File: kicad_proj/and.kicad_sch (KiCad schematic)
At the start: 2 parts, among them U7 SN74AHC1G08DBVR

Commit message: checked root, dc dc and rpi sheets
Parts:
- renumbered C16 to C17, U7 to U8
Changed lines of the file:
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@@
 		(dnp no)
 		(fields_autoplaced yes)
-		(property "Reference" "#PWR37"
+		(property "Reference" "#PWR38"
 			(at 139.7 92.71 0)
 			(effects
@@
 			(project "rpi_power_warden_hat"
 				(path "/8692c5de-a943-41e8-8e29-f6c5e99cda34/67c50b5c-a842-43c6-be7c-97015e7e2432"
-					(reference "#PWR39")
+					(reference "#PWR38")
 					(unit 1)
 				)
 				(path "/8692c5de-a943-41e8-8e29-f6c5e99cda34/fdee896d-a6fa-4854-a7d2-28092c85ff44"
-					(reference "#PWR37")
+					(reference "#PWR36")
 					(unit 1)
 				)
@@
 		(dnp no)
 		(fields_autoplaced yes)
-		(property "Reference" "#PWR38"
+		(property "Reference" "#PWR39"
 			(at 148.59 115.57 0)
 			(effects
@@
 			(project "rpi_power_warden_hat"
 				(path "/8692c5de-a943-41e8-8e29-f6c5e99cda34/67c50b5c-a842-43c6-be7c-97015e7e2432"
-					(reference "#PWR40")
+					(reference "#PWR39")
 					(unit 1)
 				)
 				(path "/8692c5de-a943-41e8-8e29-f6c5e99cda34/fdee896d-a6fa-4854-a7d2-28092c85ff44"
-					(reference "#PWR38")
+					(reference "#PWR37")
 					(unit 1)
 				)
@@
 		(on_board yes)
 		(dnp no)
-		(property "Reference" "C16"
+		(property "Reference" "C17"
 			(at 135.382 82.55 90)
 			(effects
@@
 		(dnp no)
 		(fields_autoplaced yes)
-		(property "Reference" "U7"
+		(property "Reference" "U8"
 			(at 166.37 93.0908 0)
 			(effects

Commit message: re-annotate schematic
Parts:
- renumbered U8 to U10
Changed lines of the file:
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@@
 		(dnp no)
 		(fields_autoplaced yes)
-		(property "Reference" "#PWR38"
+		(property "Reference" "#PWR42"
 			(at 139.7 92.71 0)
 			(effects
@@
 			(project "rpi_power_warden_hat"
 				(path "/8692c5de-a943-41e8-8e29-f6c5e99cda34/67c50b5c-a842-43c6-be7c-97015e7e2432"
-					(reference "#PWR38")
+					(reference "#PWR42")
 					(unit 1)
 				)
 				(path "/8692c5de-a943-41e8-8e29-f6c5e99cda34/fdee896d-a6fa-4854-a7d2-28092c85ff44"
-					(reference "#PWR36")
+					(reference "#PWR40")
 					(unit 1)
 				)
@@
 		(dnp no)
 		(fields_autoplaced yes)
-		(property "Reference" "#PWR39"
+		(property "Reference" "#PWR43"
 			(at 148.59 115.57 0)
 			(effects
@@
 			(project "rpi_power_warden_hat"
 				(path "/8692c5de-a943-41e8-8e29-f6c5e99cda34/67c50b5c-a842-43c6-be7c-97015e7e2432"
-					(reference "#PWR39")
+					(reference "#PWR43")
 					(unit 1)
 				)
 				(path "/8692c5de-a943-41e8-8e29-f6c5e99cda34/fdee896d-a6fa-4854-a7d2-28092c85ff44"
-					(reference "#PWR37")
+					(reference "#PWR41")
 					(unit 1)
 				)
@@
 		(dnp no)
 		(fields_autoplaced yes)
-		(property "Reference" "U8"
+		(property "Reference" "U10"
 			(at 166.37 93.0908 0)
 			(effects
@@
 			(project "rpi_power_warden_hat"
 				(path "/8692c5de-a943-41e8-8e29-f6c5e99cda34/67c50b5c-a842-43c6-be7c-97015e7e2432"
-					(reference "U8")
+					(reference "U10")
 					(unit 1)
 				)
 				(path "/8692c5de-a943-41e8-8e29-f6c5e99cda34/fdee896d-a6fa-4854-a7d2-28092c85ff44"
-					(reference "U7")
-					(unit 1)
-				)
+					(reference "U9")
+					(unit 1)
+				)

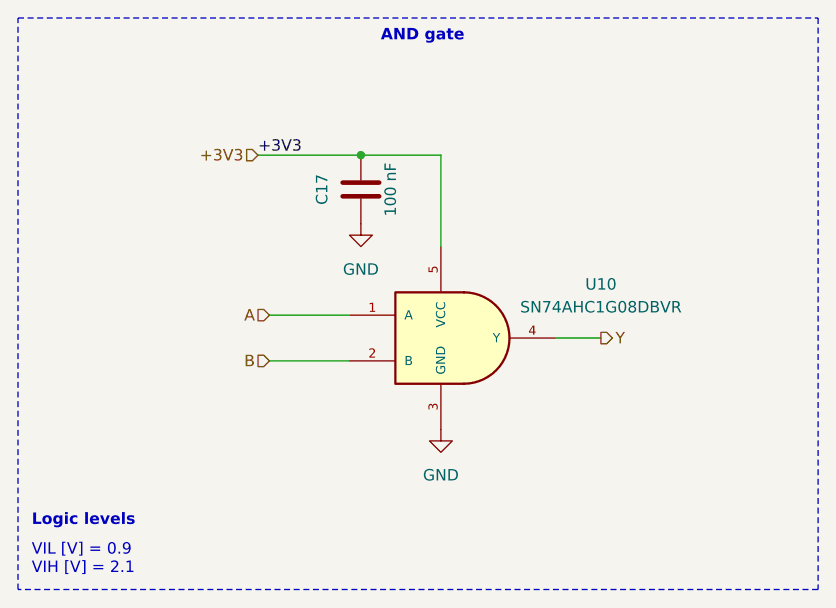
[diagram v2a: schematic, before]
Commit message: replaced almost all the components out of stock (only tensility connectors: USB and jack needs to be replaced)
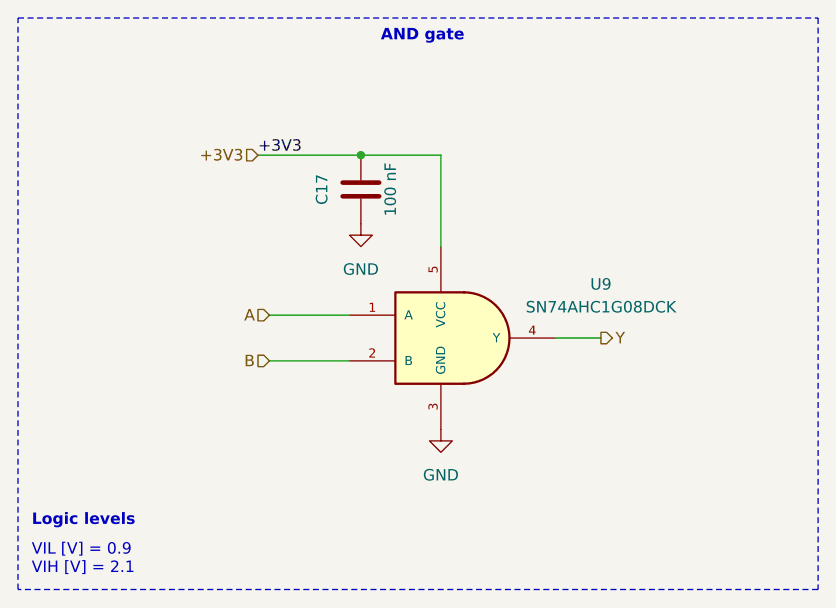
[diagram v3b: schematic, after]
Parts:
- removed U10: SN74AHC1G08DBVR, rpi_power_warden_hat:SOT-23-5, symbol rpi_power_warden_hat:SN74AHC1G08DBVR
- added U9: SN74AHC1G08DCK, rpi_power_warden_hat:SOT-353, symbol rpi_power_warden_hat:SN74AHC1G08DCK
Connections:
- net +3V3: now also U9.5 (VCC)
- net A: now also U9.1 (A)
- net B: now also U9.2 (B)
- net GND: now also U9.3 (GND)
- net Y: now also U9.4 (Y)
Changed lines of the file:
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@@
+	)
+	(symbol
+		(lib_id "rpi_power_warden_hat:SN74AHC1G08DCK")
+		(at 151.13 99.06 0)
+		(unit 1)
+		(exclude_from_sim no)
+		(in_bom yes)
+		(on_board yes)
+		(dnp no)
+		(fields_autoplaced yes)
+		(property "Reference" "U9"
+			(at 166.37 93.0908 0)
+			(effects
+				(font
+					(size 1.27 1.27)
+				)
+			)
+		)
+		(property "Value" "SN74AHC1G08DCK"
+			(at 166.37 95.6308 0)
+			(effects
+				(font
+					(size 1.27 1.27)
+				)
+			)
+		)
+		(property "Footprint" "rpi_power_warden_hat:SOT-353"
+			(at 152.908 76.454 0)
+			(effects
+				(font
+					(size 1.27 1.27)
+				)
+				(justify bottom)
+				(hide yes)
+			)
+		)
+		(property "Datasheet" "https://www.ti.com/lit/ds/symlink/sn74ahc1g08.pdf?HQS=dis-dk-null-digikeymode-dsf-pf-null-wwe&ts=1748629817144&ref_url=https%253A%252F%252Fwww.ti.com%252Fgeneral%252Fdocs%252Fsuppproductinfo.tsp%253FdistId%253D10%2526gotoUrl%253Dhttps%253A%252F%252Fwww.ti.com%252Flit%252Fgpn%252Fsn74ahc1g08"
+			(at 155.956 73.152 0)
+			(effects
+				(font
+					(size 1.27 1.27)
+				)
+				(hide yes)
+			)
+		)
+		(property "Description" "IC GATE AND 1CH 2-INP SOT23-5"
+			(at 154.178 72.898 0)
+			(effects
+				(font
+					(size 1.27 1.27)
+				)
+				(hide yes)
+			)
+		)
+		(property "mpn" "SN74AHC1G08DCK"
+			(at 152.908 76.454 0)
+			(effects
+				(font
+					(size 1.27 1.27)
+				)
+				(hide yes)
+			)
+		)
+		(property "manufacturer" "Texas Instruments"
+			(at 152.908 76.454 0)
+			(effects
+				(font
+					(size 1.27 1.27)
+				)
+				(hide yes)
+			)
+		)
+		(pin "5"
+		)
+		(pin "4"
+		)
+		(pin "2"
+		)
+		(pin "1"
+		)
+		(pin "3"
+		)
+		(instances
+			(project ""
+				(path "/8692c5de-a943-41e8-8e29-f6c5e99cda34/67c50b5c-a842-43c6-be7c-97015e7e2432"
+					(reference "U12")
+					(unit 1)
+				)
+				(path "/8692c5de-a943-41e8-8e29-f6c5e99cda34/fdee896d-a6fa-4854-a7d2-28092c85ff44"
+					(reference "U9")
+					(unit 1)
+				)
+			)
+		)
 	)
 	(symbol
@@
 					(unit 1)
 				)
-			)
-		)
-	)
-	(symbol
-		(lib_id "rpi_power_warden_hat:SN74AHC1G08DBVR")
-		(at 151.13 99.06 0)
-		(unit 1)
-		(exclude_from_sim no)
-		(in_bom yes)
-		(on_board yes)
-		(dnp no)
-		(fields_autoplaced yes)
-		(property "Reference" "U10"
-			(at 166.37 93.0908 0)
-			(effects
-				(font
-					(size 1.27 1.27)
-				)
-			)
-		)
-		(property "Value" "SN74AHC1G08DBVR"
-			(at 166.37 95.6308 0)
-			(effects
-				(font
-					(size 1.27 1.27)
-				)
-			)
-		)
-		(property "Footprint" "rpi_power_warden_hat:SOT-23-5"
-			(at 152.908 76.454 0)
-			(effects
-				(font
-					(size 1.27 1.27)
-				)
-				(justify bottom)
-				(hide yes)
-			)
-		)
-		(property "Datasheet" "https://www.ti.com/lit/ds/symlink/sn74ahc1g08.pdf?HQS=dis-dk-null-digikeymode-dsf-pf-null-wwe&ts=1748629817144&ref_url=https%253A%252F%252Fwww.ti.com%252Fgeneral%252Fdocs%252Fsuppproductinfo.tsp%253FdistId%253D10%2526gotoUrl%253Dhttps%253A%252F%252Fwww.ti.com%252Flit%252Fgpn%252Fsn74ahc1g08"
-			(at 155.956 73.152 0)
-			(effects
-				(font
-					(size 1.27 1.27)
-				)
-				(hide yes)
-			)
-		)
-		(property "Description" "IC GATE AND 1CH 2-INP SOT23-5"
-			(at 154.178 72.898 0)
-			(effects
-				(font
-					(size 1.27 1.27)
-				)
-				(hide yes)
-			)
-		)
-		(property "mpn" "SN74AHC1G08DBVR"
-			(at 152.908 76.454 0)
-			(effects
-				(font
-					(size 1.27 1.27)
-				)
-				(hide yes)
-			)
-		)
-		(property "manufacturer" "Texas Instruments"
-			(at 152.908 76.454 0)
-			(effects
-				(font
-					(size 1.27 1.27)
-				)
-				(hide yes)
-			)
-		)
-		(pin "5"
-		)
-		(pin "4"
-		)
-		(pin "2"
-		)
-		(pin "3"
-		)
-		(pin "1"
-		)
-		(instances
-			(project "rpi_power_warden_hat"
-				(path "/8692c5de-a943-41e8-8e29-f6c5e99cda34/67c50b5c-a842-43c6-be7c-97015e7e2432"
-					(reference "U10")
-					(unit 1)
-				)
-				(path "/8692c5de-a943-41e8-8e29-f6c5e99cda34/fdee896d-a6fa-4854-a7d2-28092c85ff44"
-					(reference "U9")
-					(unit 1)
-				)

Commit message: changed usb A for an usb C with more stock
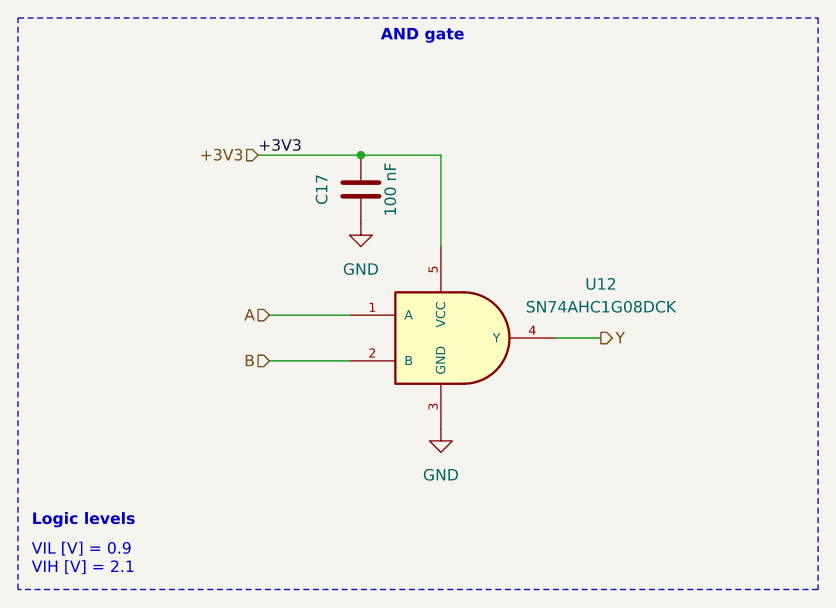
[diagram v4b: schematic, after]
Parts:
- renumbered U9 to U12
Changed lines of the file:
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@@
 		(dnp no)
 		(fields_autoplaced yes)
-		(property "Reference" "U9"
+		(property "Reference" "U12"
 			(at 166.37 93.0908 0)
 			(effects
